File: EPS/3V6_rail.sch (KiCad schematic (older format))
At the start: 14 parts

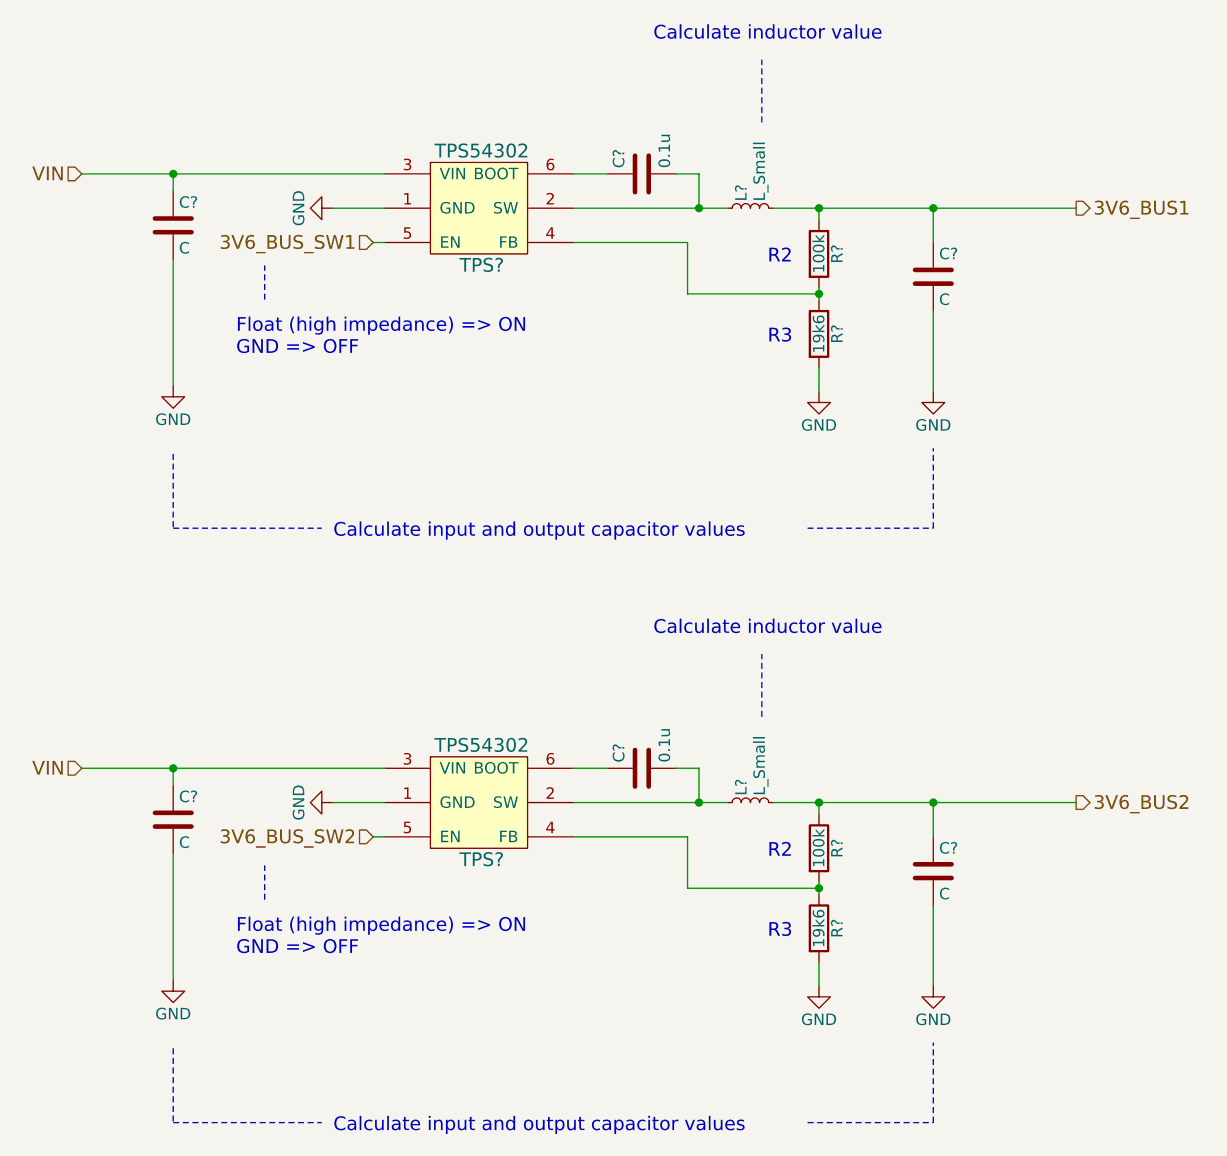
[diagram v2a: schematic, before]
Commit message: Finalized SCH (beta version) and started pcb
Capacitor banks might need to be reassigned to other locations.
No RBF pin on this SCH or PCB.
Battery gound deployment switch is fully mechanical (no mosfet switch on low side).
PCB of the prototype started. Main power converters and current measuring devices layed out.
SCH still requires ESD protection diodes!
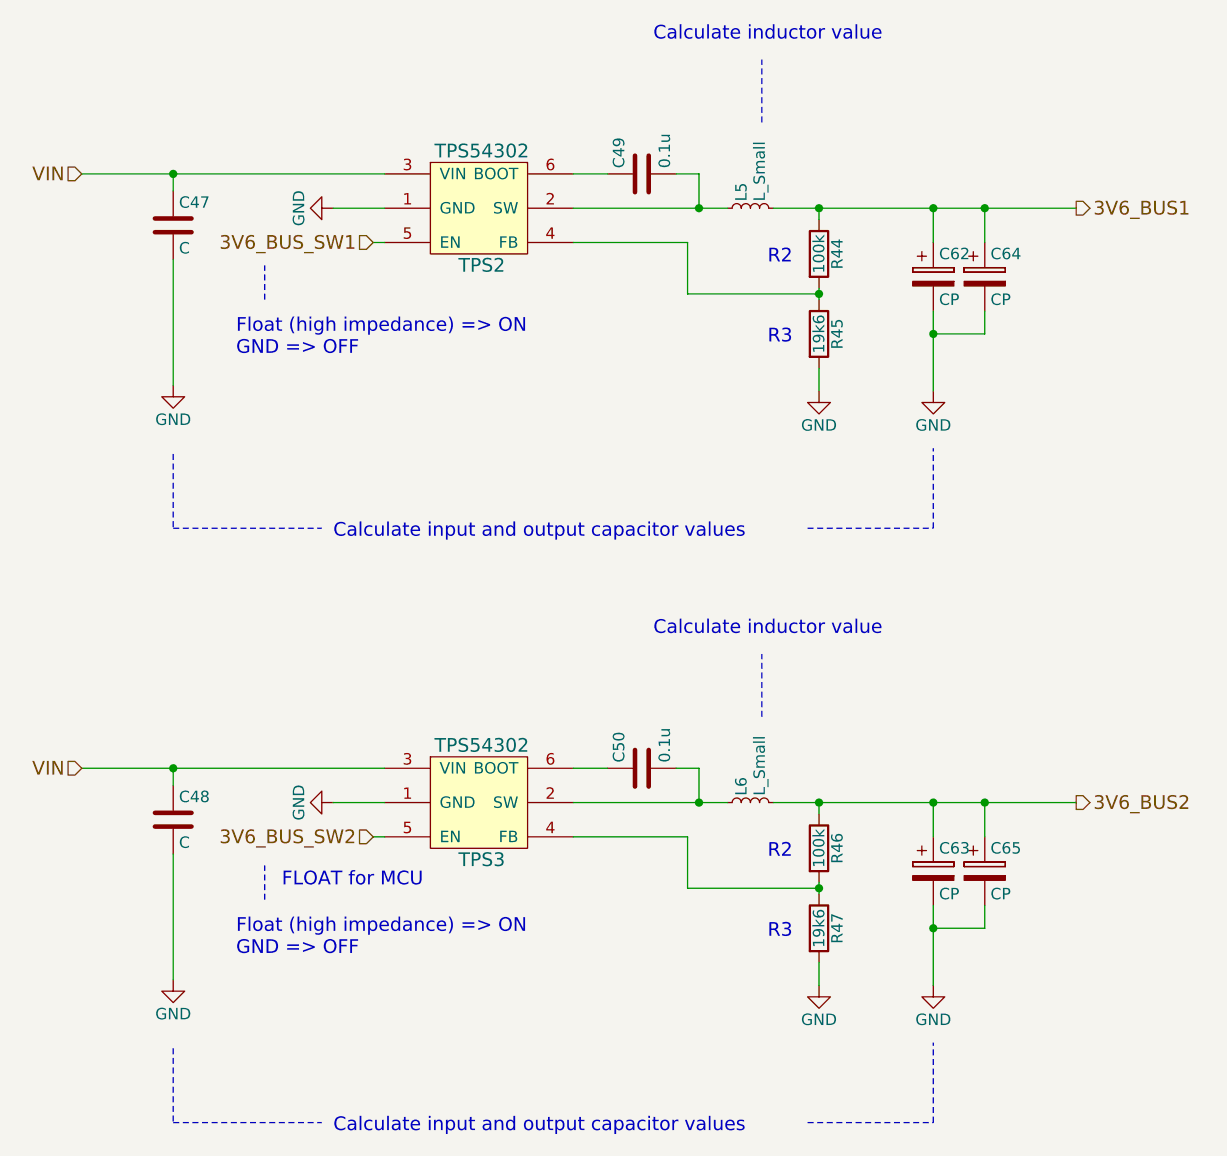
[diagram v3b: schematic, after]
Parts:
- removed C? (x2): C, symbol C
- added C62, C63, C64, C65: CP, Capacitors_Tantalum_SMD:CP_Tantalum_Case-C_EIA-6032-28_Reflow, symbol CP
- C47, C48, C49, C50: renamed from C?; footprint (none) -> Capacitors_SMD:C_0603
- L5, L6: renamed from L?; footprint (none) -> Inductors_THT:L_Axial_L7.0mm_D3.3mm_P5.08mm_Vertical_Fastron_MICC
- R44, R45, R46, R47: renamed from R?; footprint (none) -> Resistors_SMD:R_0603
- TPS2, TPS3: renamed from TPS?; footprint (none) -> TO_SOT_Packages_SMD:SOT-23-6
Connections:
- net 3V6_BUS1: now also C62.1, C64.1
- net 3V6_BUS2: now also C63.1, C65.1
- net GND: now also C62.2, C63.2, C64.2, C65.2
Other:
- note added: "FLOAT for MCU\n"
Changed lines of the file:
@@
 $Descr A4 11693 8268
 encoding utf-8
-Sheet 11 14
+Sheet 10 14
 Title "3V6 output rail"
 Date "2018-02-15"
@@
 P 5575 2000
 AR Path="/5A963D9F" Ref="TPS?"  Part="1"
-AR Path="/5A810635/5A8E9452/5A963D9F" Ref="TPS?"  Part="1"
-F 0 "TPS?" H 5600 1775 60  0000 C CNN
+AR Path="/5A810635/5A8E9452/5A963D9F" Ref="TPS2"  Part="1"
+F 0 "TPS2" H 5600 1775 60  0000 C CNN
 F 1 "TPS54302" H 5600 2275 60  0000 C CNN
-F 2 "" H 5575 1925 60  0001 C CNN
+F 2 "TO_SOT_Packages_SMD:SOT-23-6" H 5575 1925 60  0001 C CNN
 F 3 "" H 5575 1925 60  0001 C CNN
 	1    5575 2000
@@
 $EndComp
 $Comp
-L C C?
+L C C49
 U 1 1 5A963E90
 P 6300 1825
-F 0 "C?" H 6325 1925 50  0000 L CNN
+F 0 "C49" H 6325 1925 50  0000 L CNN
 F 1 "0.1u" H 6325 1725 50  0000 L CNN
-F 2 "" H 6338 1675 50  0001 C CNN
+F 2 "Capacitors_SMD:C_0603" H 6338 1675 50  0001 C CNN
 F 3 "" H 6300 1825 50  0001 C CNN
 	1    6300 1825
@@
 $EndComp
 $Comp
-L R R?
+L R R45
 U 1 1 5A964211
 P 7075 2525
-F 0 "R?" V 7155 2525 50  0000 C CNN
+F 0 "R45" V 7155 2525 50  0000 C CNN
 F 1 "19k6" V 7075 2525 50  0000 C CNN
-F 2 "" V 7005 2525 50  0001 C CNN
+F 2 "Resistors_SMD:R_0603" V 7005 2525 50  0001 C CNN
 F 3 "" H 7075 2525 50  0001 C CNN
 	1    7075 2525
@@
 $EndComp
 $Comp
-L L_Small L?
+L L_Small L5
 U 1 1 5A964292
 P 6775 1975
-F 0 "L?" H 6805 2015 50  0000 L CNN
+F 0 "L5" H 6805 2015 50  0000 L CNN
 F 1 "L_Small" H 6805 1935 50  0000 L CNN
-F 2 "" H 6775 1975 50  0001 C CNN
+F 2 "Inductors_THT:L_Axial_L7.0mm_D3.3mm_P5.08mm_Vertical_Fastron_MICC" H 6775 1975 50  0001 C CNN
 F 3 "" H 6775 1975 50  0001 C CNN
 	1    6775 1975
@@
 $EndComp
 $Comp
-L GND #PWR?
+L GND #PWR0115
 U 1 1 5A9642EB
 P 4950 1975
-F 0 "#PWR?" H 4950 1725 50  0001 C CNN
+F 0 "#PWR0115" H 4950 1725 50  0001 C CNN
 F 1 "GND" H 4950 1825 50  0000 C CNN
 F 2 "" H 4950 1975 50  0001 C CNN
@@
 Connection ~ 6550 1975
 $Comp
-L R R?
+L R R44
 U 1 1 5A9648CA
 P 7075 2175
-F 0 "R?" V 7155 2175 50  0000 C CNN
+F 0 "R44" V 7155 2175 50  0000 C CNN
 F 1 "100k" V 7075 2175 50  0000 C CNN
-F 2 "" V 7005 2175 50  0001 C CNN
+F 2 "Resistors_SMD:R_0603" V 7005 2175 50  0001 C CNN
 F 3 "" H 7075 2175 50  0001 C CNN
 	1    7075 2175
@@
 Connection ~ 7075 2350
 $Comp
-L GND #PWR?
+L GND #PWR0116
 U 1 1 5A9649FA
 P 7075 2775
-F 0 "#PWR?" H 7075 2525 50  0001 C CNN
+F 0 "#PWR0116" H 7075 2525 50  0001 C CNN
 F 1 "GND" H 7075 2625 50  0000 C CNN
 F 2 "" H 7075 2775 50  0001 C CNN
@@
 Wire Wire Line
 	7075 1975 7075 2025
-$Comp
-L C C?
-U 1 1 5A964D1D
-P 7575 2275
-F 0 "C?" H 7600 2375 50  0000 L CNN
-F 1 "C" H 7600 2175 50  0000 L CNN
-F 2 "" H 7613 2125 50  0001 C CNN
-F 3 "" H 7575 2275 50  0001 C CNN
-	1    7575 2275
-	1    0    0    -1
-$EndComp
 Wire Wire Line
 	7575 1975 7575 2125
 Connection ~ 7075 1975
 $Comp
-L GND #PWR?
+L GND #PWR0117
 U 1 1 5A964DA5
 P 7575 2775
-F 0 "#PWR?" H 7575 2525 50  0001 C CNN
+F 0 "#PWR0117" H 7575 2525 50  0001 C CNN
 F 1 "GND" H 7575 2625 50  0000 C CNN
 F 2 "" H 7575 2775 50  0001 C CNN
@@
 Connection ~ 7575 1975
 $Comp
-L C C?
+L C C47
 U 1 1 5A9661FF
 P 4250 2050
-F 0 "C?" H 4275 2150 50  0000 L CNN
+F 0 "C47" H 4275 2150 50  0000 L CNN
 F 1 "C" H 4275 1950 50  0000 L CNN
-F 2 "" H 4288 1900 50  0001 C CNN
+F 2 "Capacitors_SMD:C_0603" H 4288 1900 50  0001 C CNN
 F 3 "" H 4250 2050 50  0001 C CNN
 	1    4250 2050
@@
 	3850 1825 5175 1825
 $Comp
-L GND #PWR?
+L GND #PWR0118
 U 1 1 5A966373
 P 4250 2750
-F 0 "#PWR?" H 4250 2500 50  0001 C CNN
+F 0 "#PWR0118" H 4250 2500 50  0001 C CNN
 F 1 "GND" H 4250 2600 50  0000 C CNN
 F 2 "" H 4250 2750 50  0001 C CNN
@@
 P 5575 4600
 AR Path="/5A96903F" Ref="TPS?"  Part="1"
-AR Path="/5A810635/5A8E9452/5A96903F" Ref="TPS?"  Part="1"
-F 0 "TPS?" H 5600 4375 60  0000 C CNN
+AR Path="/5A810635/5A8E9452/5A96903F" Ref="TPS3"  Part="1"
+F 0 "TPS3" H 5600 4375 60  0000 C CNN
 F 1 "TPS54302" H 5600 4875 60  0000 C CNN
-F 2 "" H 5575 4525 60  0001 C CNN
+F 2 "TO_SOT_Packages_SMD:SOT-23-6" H 5575 4525 60  0001 C CNN
 F 3 "" H 5575 4525 60  0001 C CNN
 	1    5575 4600
@@
 $EndComp
 $Comp
-L C C?
+L C C50
 U 1 1 5A969045
 P 6300 4425
-F 0 "C?" H 6325 4525 50  0000 L CNN
+F 0 "C50" H 6325 4525 50  0000 L CNN
 F 1 "0.1u" H 6325 4325 50  0000 L CNN
-F 2 "" H 6338 4275 50  0001 C CNN
+F 2 "Capacitors_SMD:C_0603" H 6338 4275 50  0001 C CNN
 F 3 "" H 6300 4425 50  0001 C CNN
 	1    6300 4425
@@
 $EndComp
 $Comp
-L R R?
+L R R47
 U 1 1 5A96904B
 P 7075 5125
-F 0 "R?" V 7155 5125 50  0000 C CNN
+F 0 "R47" V 7155 5125 50  0000 C CNN
 F 1 "19k6" V 7075 5125 50  0000 C CNN
-F 2 "" V 7005 5125 50  0001 C CNN
+F 2 "Resistors_SMD:R_0603" V 7005 5125 50  0001 C CNN
 F 3 "" H 7075 5125 50  0001 C CNN
 	1    7075 5125
@@
 $EndComp
 $Comp
-L L_Small L?
+L L_Small L6
 U 1 1 5A969051
 P 6775 4575
-F 0 "L?" H 6805 4615 50  0000 L CNN
+F 0 "L6" H 6805 4615 50  0000 L CNN
 F 1 "L_Small" H 6805 4535 50  0000 L CNN
-F 2 "" H 6775 4575 50  0001 C CNN
+F 2 "Inductors_THT:L_Axial_L7.0mm_D3.3mm_P5.08mm_Vertical_Fastron_MICC" H 6775 4575 50  0001 C CNN
 F 3 "" H 6775 4575 50  0001 C CNN
 	1    6775 4575
@@
 $EndComp
 $Comp
-L GND #PWR?
+L GND #PWR0119
 U 1 1 5A969057
 P 4950 4575
-F 0 "#PWR?" H 4950 4325 50  0001 C CNN
+F 0 "#PWR0119" H 4950 4325 50  0001 C CNN
 F 1 "GND" H 4950 4425 50  0000 C CNN
 F 2 "" H 4950 4575 50  0001 C CNN
@@
 Connection ~ 6550 4575
 $Comp
-L R R?
+L R R46
 U 1 1 5A969062
 P 7075 4775
-F 0 "R?" V 7155 4775 50  0000 C CNN
+F 0 "R46" V 7155 4775 50  0000 C CNN
 F 1 "100k" V 7075 4775 50  0000 C CNN
-F 2 "" V 7005 4775 50  0001 C CNN
+F 2 "Resistors_SMD:R_0603" V 7005 4775 50  0001 C CNN
 F 3 "" H 7075 4775 50  0001 C CNN
 	1    7075 4775
@@
 Connection ~ 7075 4950
 $Comp
-L GND #PWR?
+L GND #PWR0120
 U 1 1 5A96906D
 P 7075 5375
-F 0 "#PWR?" H 7075 5125 50  0001 C CNN
+F 0 "#PWR0120" H 7075 5125 50  0001 C CNN
 F 1 "GND" H 7075 5225 50  0000 C CNN
 F 2 "" H 7075 5375 50  0001 C CNN
@@
 Wire Wire Line
 	7075 4575 7075 4625
-$Comp
-L C C?
-U 1 1 5A969076
-P 7575 4875
-F 0 "C?" H 7600 4975 50  0000 L CNN
-F 1 "C" H 7600 4775 50  0000 L CNN
-F 2 "" H 7613 4725 50  0001 C CNN
-F 3 "" H 7575 4875 50  0001 C CNN
-	1    7575 4875
-	1    0    0    -1
-$EndComp
 Wire Wire Line
 	7575 4575 7575 4725
 Connection ~ 7075 4575
 $Comp
-L GND #PWR?
+L GND #PWR0121
 U 1 1 5A96907E
 P 7575 5375
-F 0 "#PWR?" H 7575 5125 50  0001 C CNN
+F 0 "#PWR0121" H 7575 5125 50  0001 C CNN
 F 1 "GND" H 7575 5225 50  0000 C CNN
 F 2 "" H 7575 5375 50  0001 C CNN
@@
 	1    0    0    -1
 $EndComp
-Wire Wire Line
-	7575 5375 7575 5025
 Wire Notes Line
 	6825 4200 6825 3925
@@
 Connection ~ 7575 4575
 $Comp
-L C C?
+L C C48
 U 1 1 5A96908B
 P 4250 4650
-F 0 "C?" H 4275 4750 50  0000 L CNN
+F 0 "C48" H 4275 4750 50  0000 L CNN
 F 1 "C" H 4275 4550 50  0000 L CNN
-F 2 "" H 4288 4500 50  0001 C CNN
+F 2 "Capacitors_SMD:C_0603" H 4288 4500 50  0001 C CNN
 F 3 "" H 4250 4650 50  0001 C CNN
 	1    4250 4650
@@
 	3850 4425 5175 4425
 $Comp
-L GND #PWR?
+L GND #PWR0122
 U 1 1 5A969092
 P 4250 5350
-F 0 "#PWR?" H 4250 5100 50  0001 C CNN
+F 0 "#PWR0122" H 4250 5100 50  0001 C CNN
 F 1 "GND" H 4250 5200 50  0000 C CNN
 F 2 "" H 4250 5350 50  0001 C CNN
@@
 Wire Notes Line
 	4650 5000 4650 4850
+Text Notes 4725 4950 0    60   ~ 0
+FLOAT for MCU\n
+$Comp
+L CP C62
+U 1 1 5A96A4F4
+P 7575 2275
+F 0 "C62" H 7600 2375 50  0000 L CNN
+F 1 "CP" H 7600 2175 50  0000 L CNN
+F 2 "Capacitors_Tantalum_SMD:CP_Tantalum_Case-C_EIA-6032-28_Reflow" H 7613 2125 50  0001 C CNN
+F 3 "" H 7575 2275 50  0001 C CNN
+	1    7575 2275
+	1    0    0    -1
+$EndComp
+$Comp
+L CP C64
+U 1 1 5A96A59C
+P 7800 2275
+F 0 "C64" H 7825 2375 50  0000 L CNN
+F 1 "CP" H 7825 2175 50  0000 L CNN
+F 2 "Capacitors_Tantalum_SMD:CP_Tantalum_Case-C_EIA-6032-28_Reflow" H 7838 2125 50  0001 C CNN
+F 3 "" H 7800 2275 50  0001 C CNN
+	1    7800 2275
+	1    0    0    -1
+$EndComp
+Wire Wire Line
+	7800 2125 7800 1975
+Connection ~ 7800 1975
+Wire Wire Line
+	7800 2425 7800 2525
+Wire Wire Line
+	7800 2525 7575 2525
+Connection ~ 7575 2525
+Wire Wire Line
+	7575 5375 7575 5025
+$Comp
+L CP C63
+U 1 1 5A96A6DC
+P 7575 4875
+F 0 "C63" H 7600 4975 50  0000 L CNN
+F 1 "CP" H 7600 4775 50  0000 L CNN
+F 2 "Capacitors_Tantalum_SMD:CP_Tantalum_Case-C_EIA-6032-28_Reflow" H 7613 4725 50  0001 C CNN
+F 3 "" H 7575 4875 50  0001 C CNN
+	1    7575 4875
+	1    0    0    -1
+$EndComp
+$Comp
+L CP C65
+U 1 1 5A96A6E2
+P 7800 4875
+F 0 "C65" H 7825 4975 50  0000 L CNN
+F 1 "CP" H 7825 4775 50  0000 L CNN
+F 2 "Capacitors_Tantalum_SMD:CP_Tantalum_Case-C_EIA-6032-28_Reflow" H 7838 4725 50  0001 C CNN
+F 3 "" H 7800 4875 50  0001 C CNN
+	1    7800 4875
+	1    0    0    -1
+$EndComp
+Wire Wire Line
+	7800 5125 7800 5025
+Wire Wire Line
+	7800 4725 7800 4575
+Connection ~ 7800 4575
+Wire Wire Line
+	7575 5125 7800 5125
+Connection ~ 7575 5125
 $EndSCHEMATC
